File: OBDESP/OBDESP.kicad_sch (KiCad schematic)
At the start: 39 parts, among them J1 USB_A, J2 RST, J3 BOOT, J4 UART, Q1 BC848CLT1G, U1 NCP1117-3.3_DPAK, U2 ESP32-WROOM-32, U3 NRF24L01_SMD

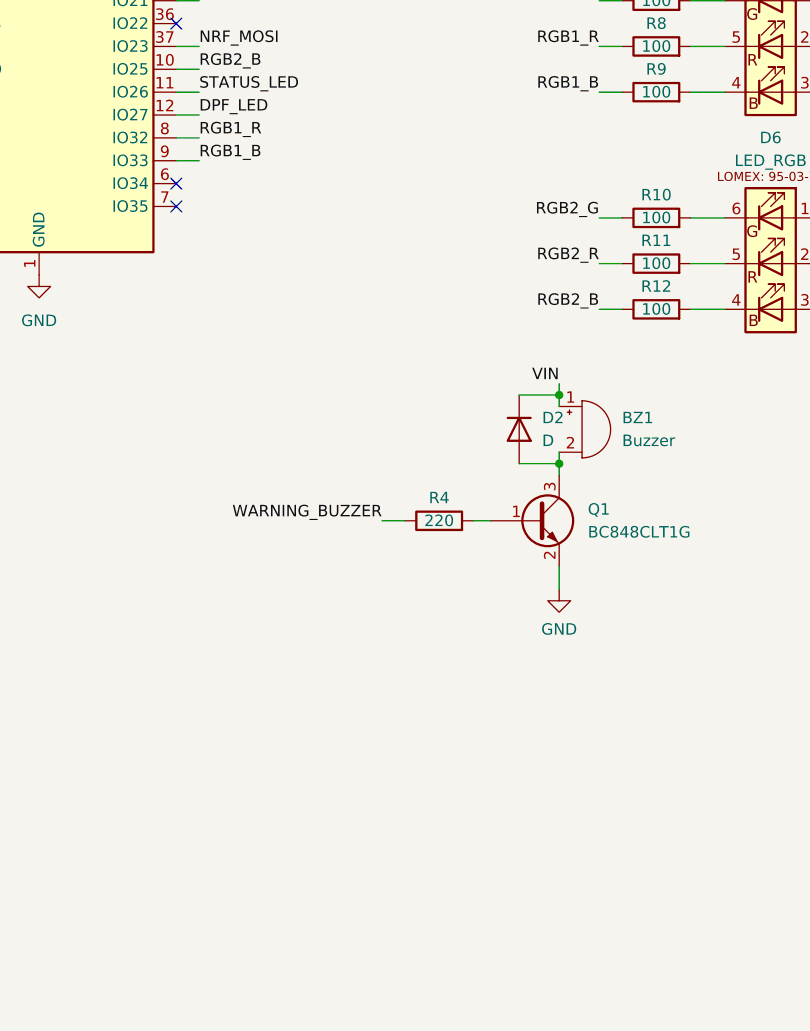
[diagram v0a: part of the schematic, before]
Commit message: Updated both PCBs with TEMT6000 and XKC enabler
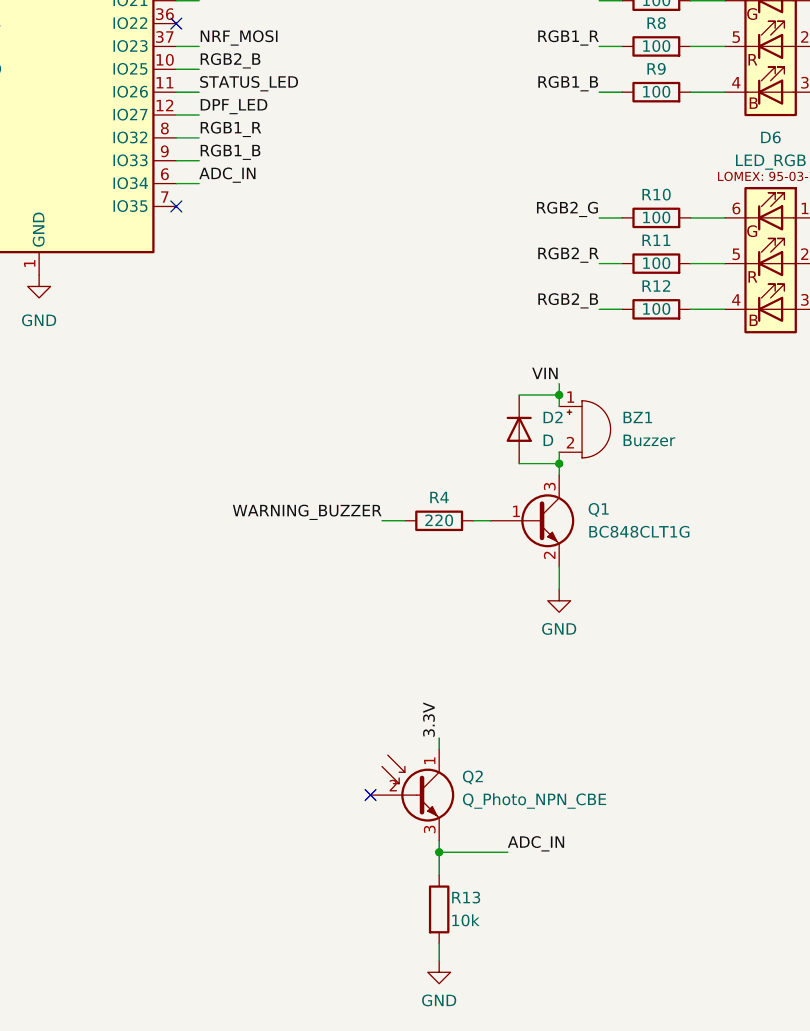
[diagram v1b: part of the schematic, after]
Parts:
- added Q2: Q_Photo_NPN_CBE, mykicad_6:TEMT6000, symbol Device:Q_Photo_NPN_CBE
- added R13: 10k, Resistor_SMD:R_0603_1608Metric, symbol Device:R
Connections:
- net 3.3V: now also Q2.1 (C)
- net GND: now also R13.2
- net ADC_IN: now reaches U2.6 (IO34)
- net ADC_IN: now also Q2.3 (E), R13.1
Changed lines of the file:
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@@
   (junction (at 93.98 27.94) (diameter 0) (color 0 0 0 0)
+  )
+  (junction (at 138.43 170.815) (diameter 0) (color 0 0 0 0)
   )
   (junction (at 184.15 105.41) (diameter 0) (color 0 0 0 0)
@@
   (no_connect (at 55.88 83.82))
   (no_connect (at 72.39 142.24))
+  (no_connect (at 130.81 164.465))
+  (no_connect (at 109.22 63.5))
   (no_connect (at 109.22 60.96))
   (no_connect (at 109.22 99.06))
@@
   (no_connect (at 55.88 86.36))
   (no_connect (at 109.22 78.74))
-  (no_connect (at 109.22 63.5))
-  (no_connect (at 109.22 96.52))
   (no_connect (at 109.22 45.72))
   (no_connect (at 78.74 48.26))
@@
     (stroke (width 0) (type default) (color 0 0 0 0))
   )
+  (wire (pts (xy 138.43 170.815) (xy 138.43 173.355))
+    (stroke (width 0) (type default) (color 0 0 0 0))
+  )
   (wire (pts (xy 109.22 86.36) (xy 111.76 86.36))
     (stroke (width 0) (type default) (color 0 0 0 0))
@@
     (stroke (width 0) (type default) (color 0 0 0 0))
   )
+  (wire (pts (xy 138.43 158.115) (xy 138.43 159.385))
+    (stroke (width 0) (type default) (color 0 0 0 0))
+  )
   (wire (pts (xy 166.37 100.33) (xy 170.18 100.33))
     (stroke (width 0) (type default) (color 0 0 0 0))
@@
     (stroke (width 0) (type default) (color 0 0 0 0))
   )
+  (wire (pts (xy 138.43 170.815) (xy 146.05 170.815))
+    (stroke (width 0) (type default) (color 0 0 0 0))
+  )
   (wire (pts (xy 166.37 110.49) (xy 170.18 110.49))
     (stroke (width 0) (type default) (color 0 0 0 0))
@@
     (stroke (width 0) (type default) (color 0 0 0 0))
   )
+  (wire (pts (xy 111.76 96.52) (xy 109.22 96.52))
+    (stroke (width 0) (type default) (color 0 0 0 0))
+  )
   (wire (pts (xy 114.3 53.34) (xy 114.3 57.785))
     (stroke (width 0) (type default) (color 0 0 0 0))
   )
+  (wire (pts (xy 138.43 180.975) (xy 138.43 182.88))
+    (stroke (width 0) (type default) (color 0 0 0 0))
+  )
   (wire (pts (xy 166.37 55.88) (xy 171.45 55.88))
     (stroke (width 0) (type default) (color 0 0 0 0))
@@
   )
   (wire (pts (xy 180.34 105.41) (xy 184.15 105.41))
+    (stroke (width 0) (type default) (color 0 0 0 0))
+  )
+  (wire (pts (xy 138.43 169.545) (xy 138.43 170.815))
     (stroke (width 0) (type default) (color 0 0 0 0))
   )
@@
     (effects (font (size 1.27 1.27)) (justify left bottom))
   )
+  (label "ADC_IN" (at 111.76 96.52 0)
+    (effects (font (size 1.27 1.27)) (justify left bottom))
+  )
   (label "NRF_CSN" (at 52.07 142.24 180)
     (effects (font (size 1.27 1.27)) (justify right bottom))
   )
+  (label "ADC_IN" (at 146.05 170.815 0)
+    (effects (font (size 1.27 1.27)) (justify left bottom))
+  )
   (label "3.3V" (at 187.96 76.2 0)
     (effects (font (size 1.27 1.27)) (justify left bottom))
@@
   (label "3.3V" (at 39.37 132.08 180)
     (effects (font (size 1.27 1.27)) (justify right bottom))
+  )
+  (label "3.3V" (at 138.43 158.115 90)
+    (effects (font (size 1.27 1.27)) (justify left bottom))
   )
   (label "WARNING_BUZZER" (at 132.08 133.985 180)
@@
     (pin "5")
     (pin "6")
+  )
+  (symbol (lib_id "Device:R") (at 138.43 177.165 0) (unit 1)
+    (in_bom yes) (on_board yes)
+    (property "Reference" "R13" (id 0) (at 139.7 175.895 0)
+      (effects (font (size 1.27 1.27)) (justify left))
+    )
+    (property "Value" "10k" (id 1) (at 139.7 178.435 0)
+      (effects (font (size 1.27 1.27)) (justify left))
+    )
+    (property "Footprint" "Resistor_SMD:R_0603_1608Metric" (id 2) (at 136.652 177.165 90)
+      (effects (font (size 1.27 1.27)) hide)
+    )
+    (property "Datasheet" "~" (id 3) (at 138.43 177.165 0)
+      (effects (font (size 1.27 1.27)) hide)
+    )
+    (property "LOMEX" "81-35-56" (id 4) (at 138.43 177.165 0)
+      (effects (font (size 1.27 1.27)) hide)
+    )
+    (pin "1")
+    (pin "2")
   )
   (symbol (lib_id "power:GND") (at 51.435 138.43 270) (unit 1)
@@
     (pin "2")
   )
+  (symbol (lib_id "Device:Q_Photo_NPN_CBE") (at 135.89 164.465 0) (unit 1)
+    (in_bom yes) (on_board yes) (fields_autoplaced)
+    (property "Reference" "Q2" (id 0) (at 140.97 162.4456 0)
+      (effects (font (size 1.27 1.27)) (justify left))
+    )
+    (property "Value" "Q_Photo_NPN_CBE" (id 1) (at 140.97 164.9856 0)
+      (effects (font (size 1.27 1.27)) (justify left))
+    )
+    (property "Footprint" "mykicad_6:TEMT6000" (id 2) (at 140.97 161.925 0)
+      (effects (font (size 1.27 1.27)) hide)
+    )
+    (property "Datasheet" "~" (id 3) (at 135.89 164.465 0)
+      (effects (font (size 1.27 1.27)) hide)
+    )
+    (property "mouser" "78-TEMT6000" (id 4) (at 135.89 164.465 0)
+      (effects (font (size 1.27 1.27)) hide)
+    )
+    (pin "1")
+    (pin "2")
+    (pin "3")
+  )
   (symbol (lib_id "Device:R") (at 162.56 55.88 90) (unit 1)
     (in_bom yes) (on_board yes)
@@
     (pin "1")
   )
+  (symbol (lib_id "power:GND") (at 138.43 182.88 0) (unit 1)
+    (in_bom yes) (on_board yes) (fields_autoplaced)
+    (property "Reference" "#PWR0115" (id 0) (at 138.43 189.23 0)
+      (effects (font (size 1.27 1.27)) hide)
+    )
+    (property "Value" "GND" (id 1) (at 138.43 187.325 0))
+    (property "Footprint" "" (id 2) (at 138.43 182.88 0)
+      (effects (font (size 1.27 1.27)) hide)
+    )
+    (property "Datasheet" "" (id 3) (at 138.43 182.88 0)
+      (effects (font (size 1.27 1.27)) hide)
+    )
+    (pin "1")
+  )
   (symbol (lib_id "Device:LED") (at 175.26 55.88 0) (unit 1)
     (in_bom yes) (on_board yes) (fields_autoplaced)
@@
       (reference "#PWR0114") (unit 1) (value "GND") (footprint "")
     )
+    (path "/f42ad2d2-1043-4ed3-bf3c-62a34d75876c"
+      (reference "#PWR0115") (unit 1) (value "GND") (footprint "")
+    )
     (path "/11e87e56-f960-4218-a54e-4dde14cdfc1e"
       (reference "BZ1") (unit 1) (value "Buzzer") (footprint "Buzzer_Beeper:PUIAudio_SMT_0825_S_4_R")
@@
       (reference "Q1") (unit 1) (value "BC848CLT1G") (footprint "Package_TO_SOT_SMD:SOT-23")
     )
+    (path "/b16727ba-bed3-4eda-abf0-5162487b5da0"
+      (reference "Q2") (unit 1) (value "Q_Photo_NPN_CBE") (footprint "mykicad_6:TEMT6000")
+    )
     (path "/f9720149-0212-47d0-976d-f910d4913cf7"
       (reference "R1") (unit 1) (value "10k") (footprint "Resistor_SMD:R_0603_1608Metric")
@@
       (reference "R12") (unit 1) (value "100") (footprint "Resistor_SMD:R_0603_1608Metric")
     )
+    (path "/33d13857-75db-4875-b9c6-3f45ac962845"
+      (reference "R13") (unit 1) (value "10k") (footprint "Resistor_SMD:R_0603_1608Metric")
+    )
     (path "/221a80d8-498b-4c3c-a7aa-429f5de6e9cd"

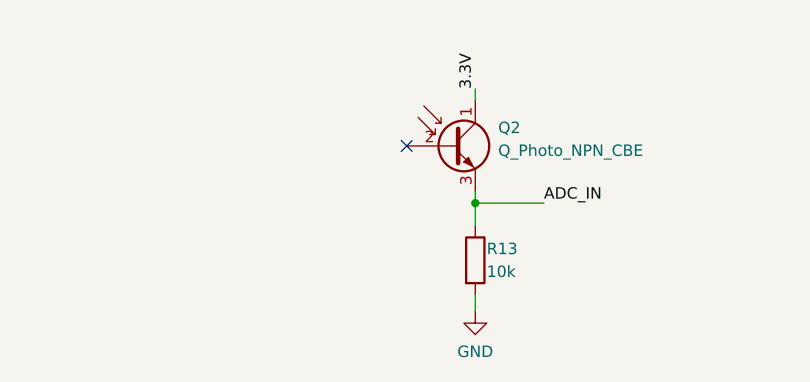
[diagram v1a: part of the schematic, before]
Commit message: ESP32-added ADC functions untested! PCB update
added capacitor for PCB design for ADC reading the TEMT6000 sensor
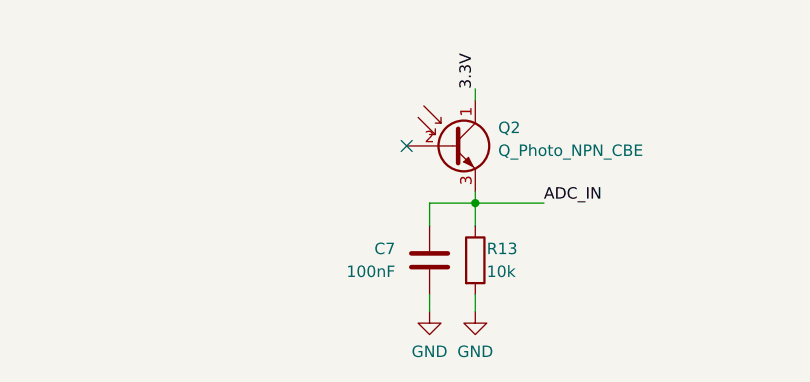
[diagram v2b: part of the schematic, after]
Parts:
- added C7: 100nF, Capacitor_SMD:C_0603_1608Metric, symbol Device:C
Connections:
- net ADC_IN: now also C7.2
- net GND: now also C7.1
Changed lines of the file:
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@@
+    (stroke (width 0) (type default) (color 0 0 0 0))
+  )
+  (wire (pts (xy 138.43 170.815) (xy 133.35 170.815))
     (stroke (width 0) (type default) (color 0 0 0 0))
   )
@@
     (stroke (width 0) (type default) (color 0 0 0 0))
   )
+  (wire (pts (xy 133.35 170.815) (xy 133.35 173.355))
+    (stroke (width 0) (type default) (color 0 0 0 0))
+  )
   (wire (pts (xy 71.12 30.48) (xy 71.12 33.02))
     (stroke (width 0) (type default) (color 0 0 0 0))
@@
   )
   (wire (pts (xy 110.49 58.42) (xy 110.49 62.865))
+    (stroke (width 0) (type default) (color 0 0 0 0))
+  )
+  (wire (pts (xy 133.35 180.975) (xy 133.35 182.88))
     (stroke (width 0) (type default) (color 0 0 0 0))
   )
@@
     )
   )
+  (symbol (lib_id "Device:C") (at 133.35 177.165 180) (unit 1)
+    (in_bom yes) (on_board yes) (fields_autoplaced)
+    (property "Reference" "C7" (id 0) (at 129.54 175.8949 0)
+      (effects (font (size 1.27 1.27)) (justify left))
+    )
+    (property "Value" "100nF" (id 1) (at 129.54 178.4349 0)
+      (effects (font (size 1.27 1.27)) (justify left))
+    )
+    (property "Footprint" "Capacitor_SMD:C_0603_1608Metric" (id 2) (at 132.3848 173.355 0)
+      (effects (font (size 1.27 1.27)) hide)
+    )
+    (property "Datasheet" "~" (id 3) (at 133.35 177.165 0)
+      (effects (font (size 1.27 1.27)) hide)
+    )
+    (property "LOMEX" "82-13-28" (id 4) (at 133.35 177.165 0)
+      (effects (font (size 1.27 1.27)) hide)
+    )
+    (pin "1")
+    (pin "2")
+  )
   (symbol (lib_id "Connector_Generic:Conn_01x04") (at 125.73 45.72 0) (unit 1)
     (in_bom yes) (on_board yes) (fields_autoplaced)
@@
     (pin "2")
   )
+  (symbol (lib_id "power:GND") (at 133.35 182.88 0) (unit 1)
+    (in_bom yes) (on_board yes) (fields_autoplaced)
+    (property "Reference" "#PWR0116" (id 0) (at 133.35 189.23 0)
+      (effects (font (size 1.27 1.27)) hide)
+    )
+    (property "Value" "GND" (id 1) (at 133.35 187.325 0))
+    (property "Footprint" "" (id 2) (at 133.35 182.88 0)
+      (effects (font (size 1.27 1.27)) hide)
+    )
+    (property "Datasheet" "" (id 3) (at 133.35 182.88 0)
+      (effects (font (size 1.27 1.27)) hide)
+    )
+    (pin "1")
+  )
   (symbol (lib_id "Mechanical:Housing") (at 224.155 57.785 0) (unit 1)
     (in_bom yes) (on_board yes) (fields_autoplaced)
@@
       (reference "#PWR0115") (unit 1) (value "GND") (footprint "")
     )
+    (path "/eb79ed3b-eb4b-4472-a313-c2099b996949"
+      (reference "#PWR0116") (unit 1) (value "GND") (footprint "")
+    )
     (path "/11e87e56-f960-4218-a54e-4dde14cdfc1e"
       (reference "BZ1") (unit 1) (value "Buzzer") (footprint "Buzzer_Beeper:PUIAudio_SMT_0825_S_4_R")
@@
       (reference "C6") (unit 1) (value "22uF") (footprint "Capacitor_Tantalum_SMD:CP_EIA-3216-18_Kemet-A")
     )
+    (path "/8a384f29-ddfd-4aa0-9363-e0056c755fca"
+      (reference "C7") (unit 1) (value "100nF") (footprint "Capacitor_SMD:C_0603_1608Metric")
+    )
     (path "/1ee37d51-25ae-4651-a95e-05fcab077038"

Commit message: minimal xls update
f
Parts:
- N1: Mouser (none) -> 546-1551USB3CLR
- Q2: Mouser (none) -> 78-TEMT6000
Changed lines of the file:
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@@
+      (effects (font (size 1.27 1.27)) hide)
+    )
+    (property "Mouser" "78-TEMT6000" (id 5) (at 135.89 164.465 0)
       (effects (font (size 1.27 1.27)) hide)
     )
@@
       (effects (font (size 1.27 1.27)) hide)
     )
+    (property "Mouser" "546-1551USB3CLR" (id 5) (at 224.155 57.785 0)
+      (effects (font (size 1.27 1.27)) hide)
+    )

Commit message: latest versions
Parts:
- removed C7: 100nF, Capacitor_SMD:C_0603_1608Metric, symbol Device:C
- removed Q2: Q_Photo_NPN_CBE, mykicad_6:TEMT6000, symbol Device:Q_Photo_NPN_CBE
- removed R13: 10k, Resistor_SMD:R_0603_1608Metric, symbol Device:R
- D3: value WHITE_LED -> YELLOW_LED; LOMEX 95-04-08 -> 95-03-07
- D4: value YELLOW_OIL_LED -> WHITE_LED; LOMEX 95-03-07 -> 95-04-08
- R10, R11, R12, R7, R8, R9: LOMEX 81-10-16 -> 80-11-53
- R6: renamed from R5; LOMEX 81-10-16 -> 80-11-53
- renumbered R6 to R5
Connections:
- net WATER_LED is gone; now on net DPF_LED: R6.1, U2.14 (IO12)
- net DPF_LED: no longer R5.1, U2.12 (IO27)
- net at D3.1 (K): now also R5.2; no longer R6.2
- net at D4.1 (K): now also R6.2; no longer R5.2
- net STATUS_LED renamed STATUS1_LED
- new net COOLANTSTATUS_LED: R5.1, U2.12 (IO27)
- no-connect marks 18 -> 17
